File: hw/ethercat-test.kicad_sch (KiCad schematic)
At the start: 0 parts

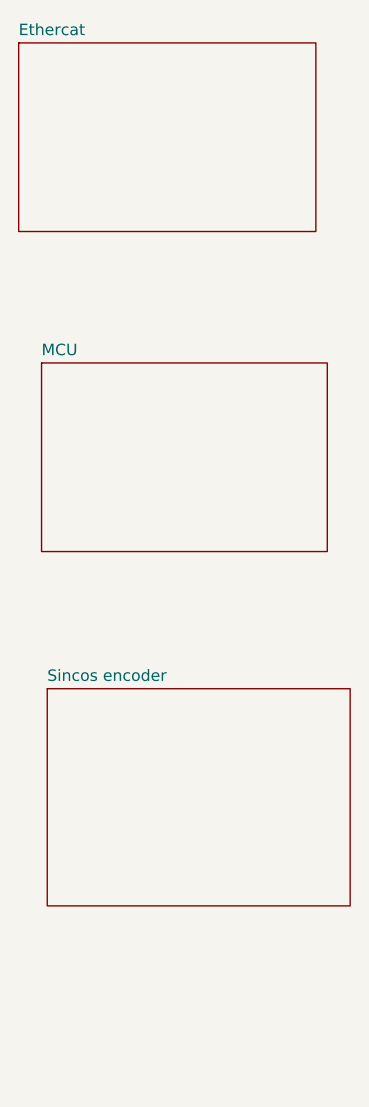
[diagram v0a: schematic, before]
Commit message: Update encoder circuit
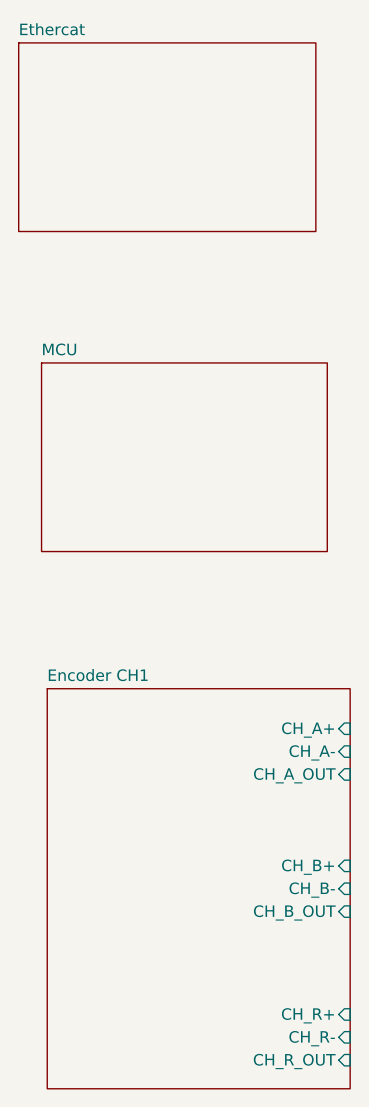
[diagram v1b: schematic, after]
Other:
- sheet Sincos encoder renamed Encoder CH1
- sheet Encoder CH1 ports: added CH_A+, CH_A-, CH_A_OUT, CH_B+, CH_B-, CH_B_OUT, CH_R+, CH_R-, CH_R_OUT; removed none
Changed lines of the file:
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@@
 	(sheet
 		(at 29.21 95.885)
-		(size 33.655 24.13)
+		(size 33.655 44.45)
 		(fields_autoplaced yes)
 		(stroke
@@
 			(color 0 0 0 0.0000)
 		)
-		(property "Sheetname" "Sincos encoder"
+		(property "Sheetname" "Encoder CH1"
 			(at 29.21 95.1734 0)
 			(effects
@@
 		)
 		(property "Sheetfile" "encoder.kicad_sch"
-			(at 29.21 120.5996 0)
+			(at 29.21 140.9196 0)
 			(effects
 				(font
@@
 			)
 		)
+		(pin "CH_A+" input
+			(at 62.865 100.33 0)
+			(effects
+				(font
+					(size 1.27 1.27)
+				)
+				(justify right)
+			)
+		)
+		(pin "CH_A-" input
+			(at 62.865 102.87 0)
+			(effects
+				(font
+					(size 1.27 1.27)
+				)
+				(justify right)
+			)
+		)
+		(pin "CH_A_OUT" input
+			(at 62.865 105.41 0)
+			(effects
+				(font
+					(size 1.27 1.27)
+				)
+				(justify right)
+			)
+		)
+		(pin "CH_B_OUT" input
+			(at 62.865 120.65 0)
+			(effects
+				(font
+					(size 1.27 1.27)
+				)
+				(justify right)
+			)
+		)
+		(pin "CH_B+" input
+			(at 62.865 115.57 0)
+			(effects
+				(font
+					(size 1.27 1.27)
+				)
+				(justify right)
+			)
+		)
+		(pin "CH_B-" input
+			(at 62.865 118.11 0)
+			(effects
+				(font
+					(size 1.27 1.27)
+				)
+				(justify right)
+			)
+		)
+		(pin "CH_R-" input
+			(at 62.865 134.62 0)
+			(effects
+				(font
+					(size 1.27 1.27)
+				)
+				(justify right)
+			)
+		)
+		(pin "CH_R+" input
+			(at 62.865 132.08 0)
+			(effects
+				(font
+					(size 1.27 1.27)
+				)
+				(justify right)
+			)
+		)
+		(pin "CH_R_OUT" input
+			(at 62.865 137.16 0)
+			(effects
+				(font
+					(size 1.27 1.27)
+				)
+				(justify right)
+			)
+		)
